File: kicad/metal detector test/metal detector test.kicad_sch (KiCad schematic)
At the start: 109 parts, among them J1 3.5mm audio jack TRS, Q1 PNP, Q2 NPN, SW1 SW_SPST, SW10 SW_SPST, SW2 SW_SPST, SW3 SW_SPST, SW4 SW_SPST, SW5 SW_SPST, SW6 SW_SPST, SW7 SW_SPST, SW8 SW_SPST, SW9 SW_SPST, U1 op amp (higher voltage), U10 3.3v lin reg, U11 lp filter, U12 op amp (lower voltage), U2 nucleo-32 uC module, U3 9v lin reg, U4 5v lin reg, U5 3.3v lin reg, U6 audio amp, U7 lp filter, U8 switch debounce, U9 5v lin reg

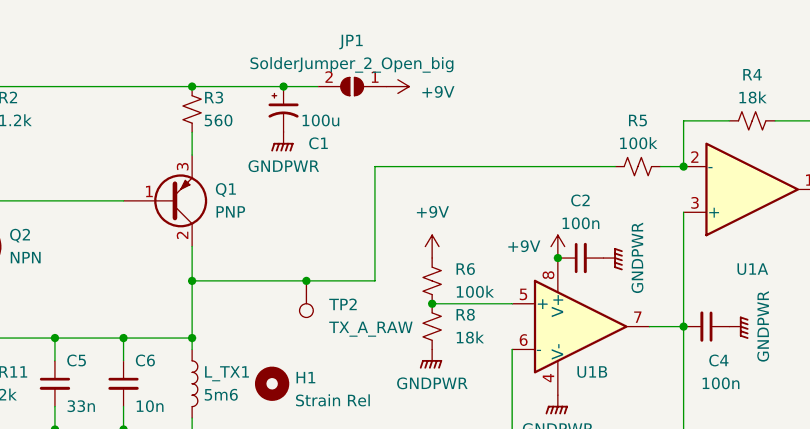
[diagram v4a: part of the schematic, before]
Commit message: Mostly positioned the parts
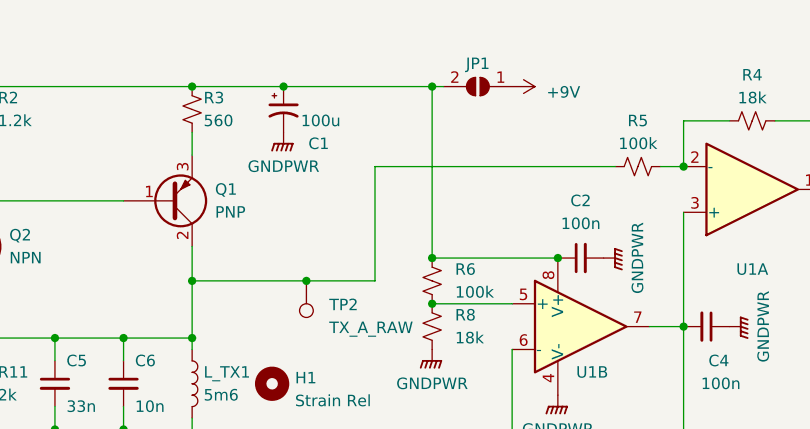
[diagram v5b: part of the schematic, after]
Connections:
- net +9V: no longer C2.1, R6.1, U1.8 (V+)
- net at C1.1, JP1.2 (B), R1.1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: now also C2.1, R6.1, U1.8 (V+)
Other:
- moved on the sheet: JP1
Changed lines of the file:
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@@
     (comment 1 "Allen Jordan, allen.jordan@gmail.com")
   )
+  (junction (at 72.39 20.32) (diameter 0) (color 0 0 0 0)
+  )
   (junction (at 45.72 48.26) (diameter 0) (color 0 0 0 0)
   )
@@
   (junction (at 22.86 20.32) (diameter 0) (color 0 0 0 0)
   )
-  (junction (at 86.36 39.37) (diameter 0) (color 0 0 0 0)
-  )
   (junction (at 109.22 100.33) (diameter 0) (color 0 0 0 0)
   )
@@
   (junction (at 40.64 90.17) (diameter 0) (color 0 0 0 0)
   )
+  (junction (at 86.36 39.37) (diameter 0) (color 0 0 0 0)
+  )
   (junction (at 247.65 110.49) (diameter 0) (color 0 0 0 0)
   )
@@
   (junction (at 240.03 48.26) (diameter 0) (color 0 0 0 0)
   )
+  (junction (at 72.39 39.37) (diameter 0) (color 0 0 0 0)
+  )
   (junction (at 38.1 58.42) (diameter 0) (color 0 0 0 0)
   )
@@
     (stroke (width 0) (type default))
   )
+  (wire (pts (xy 72.39 20.32) (xy 72.39 39.37))
+    (stroke (width 0) (type default))
+  )
   (wire (pts (xy 232.41 148.59) (xy 234.95 148.59))
     (stroke (width 0) (type default))
@@
     (stroke (width 0) (type default))
   )
-  (wire (pts (xy 59.69 20.32) (xy 55.88 20.32))
+  (wire (pts (xy 73.66 20.32) (xy 72.39 20.32))
     (stroke (width 0) (type default))
   )
@@
     (stroke (width 0) (type default))
   )
+  (wire (pts (xy 72.39 20.32) (xy 55.88 20.32))
+    (stroke (width 0) (type default))
+  )
   (wire (pts (xy 143.51 107.95) (xy 160.02 107.95))
     (stroke (width 0) (type default))
@@
     (stroke (width 0) (type default))
   )
+  (wire (pts (xy 72.39 39.37) (xy 86.36 39.37))
+    (stroke (width 0) (type default))
+  )
   (wire (pts (xy 123.19 107.95) (xy 109.22 107.95))
     (stroke (width 0) (type default))
@@
     )
   )
-  (symbol (lib_id "power:+9V") (at 67.31 20.32 270) (unit 1)
+  (symbol (lib_id "power:+9V") (at 81.28 20.32 270) (unit 1)
     (in_bom yes) (on_board yes) (dnp no) (fields_autoplaced)
-    (property "Reference" "#PWR01" (at 63.5 20.32 0)
+    (property "Reference" "#PWR01" (at 77.47 20.32 0)
       (effects (font (size 1.27 1.27)) hide)
     )
-    (property "Value" "+9V" (at 71.12 20.955 90)
+    (property "Value" "+9V" (at 85.09 20.955 90)
       (effects (font (size 1.27 1.27)) (justify left))
     )
-    (property "Footprint" "" (at 67.31 20.32 0)
+    (property "Footprint" "" (at 81.28 20.32 0)
       (effects (font (size 1.27 1.27)) hide)
     )
-    (property "Datasheet" "" (at 67.31 20.32 0)
+    (property "Datasheet" "" (at 81.28 20.32 0)
       (effects (font (size 1.27 1.27)) hide)
     )
@@
     )
   )
-  (symbol (lib_id "power:+9V") (at 86.36 39.37 0) (unit 1)
-    (in_bom yes) (on_board yes) (dnp no)
-    (property "Reference" "#PWR08" (at 86.36 43.18 0)
-      (effects (font (size 1.27 1.27)) hide)
-    )
-    (property "Value" "+9V" (at 82.55 38.1 0)
-      (effects (font (size 1.27 1.27)))
-    )
-    (property "Footprint" "" (at 86.36 39.37 0)
-      (effects (font (size 1.27 1.27)) hide)
-    )
-    (property "Datasheet" "" (at 86.36 39.37 0)
-      (effects (font (size 1.27 1.27)) hide)
-    )
-    (pin "1")
-    (instances
-      (project "metal detector test"
-        (path "/aac94249-970f-41d5-8c24-6bade512464d"
-          (reference "#PWR08") (unit 1)
-        )
-      )
-    )
-  )
   (symbol (lib_id "Device:R_Small_US") (at 17.78 48.26 270) (unit 1)
     (in_bom yes) (on_board yes) (dnp no)
@@
     )
   )
-  (symbol (lib_id "Jumper:SolderJumper_2_Open") (at 63.5 20.32 180) (unit 1)
-    (in_bom yes) (on_board yes) (dnp no) (fields_autoplaced)
-    (property "Reference" "JP1" (at 63.5 15.24 0)
+  (symbol (lib_id "Jumper:SolderJumper_2_Open") (at 77.47 20.32 180) (unit 1)
+    (in_bom yes) (on_board yes) (dnp no)
+    (property "Reference" "JP1" (at 77.47 17.78 0)
       (effects (font (size 1.27 1.27)))
     )
-    (property "Value" "SolderJumper_2_Open_big" (at 63.5 17.78 0)
-      (effects (font (size 1.27 1.27)))
+    (property "Value" "SolderJumper_2_Open_big" (at 77.47 17.78 0)
+      (effects (font (size 1.27 1.27)) hide)
     )
-    (property "Footprint" "allen footprints:SolderJumper-2_Open_big_allen" (at 63.5 20.32 0)
+    (property "Footprint" "allen footprints:SolderJumper-2_Open_big_allen" (at 77.47 20.32 0)
       (effects (font (size 1.27 1.27)) hide)
     )
-    (property "Datasheet" "~" (at 63.5 20.32 0)
+    (property "Datasheet" "~" (at 77.47 20.32 0)
       (effects (font (size 1.27 1.27)) hide)
     )
-    (property "MPN" "" (at 63.5 20.32 0)
+    (property "MPN" "" (at 77.47 20.32 0)
       (effects (font (size 1.27 1.27)) hide)
     )
@@
         )
       )
-    )
-  )
-  (symbol (lib_id "power:+9V") (at 72.39 39.37 0) (unit 1)
-    (in_bom yes) (on_board yes) (dnp no) (fields_autoplaced)
-    (property "Reference" "#PWR07" (at 72.39 43.18 0)
-      (effects (font (size 1.27 1.27)) hide)
-    )
-    (property "Value" "+9V" (at 72.39 34.29 0)
-      (effects (font (size 1.27 1.27)))
-    )
-    (property "Footprint" "" (at 72.39 39.37 0)
-      (effects (font (size 1.27 1.27)) hide)
-    )
-    (property "Datasheet" "" (at 72.39 39.37 0)
-      (effects (font (size 1.27 1.27)) hide)
-    )
-    (pin "1")
-    (instances
-      (project "metal detector test"
-        (path "/aac94249-970f-41d5-8c24-6bade512464d"
-          (reference "#PWR07") (unit 1)
-        )
-      )

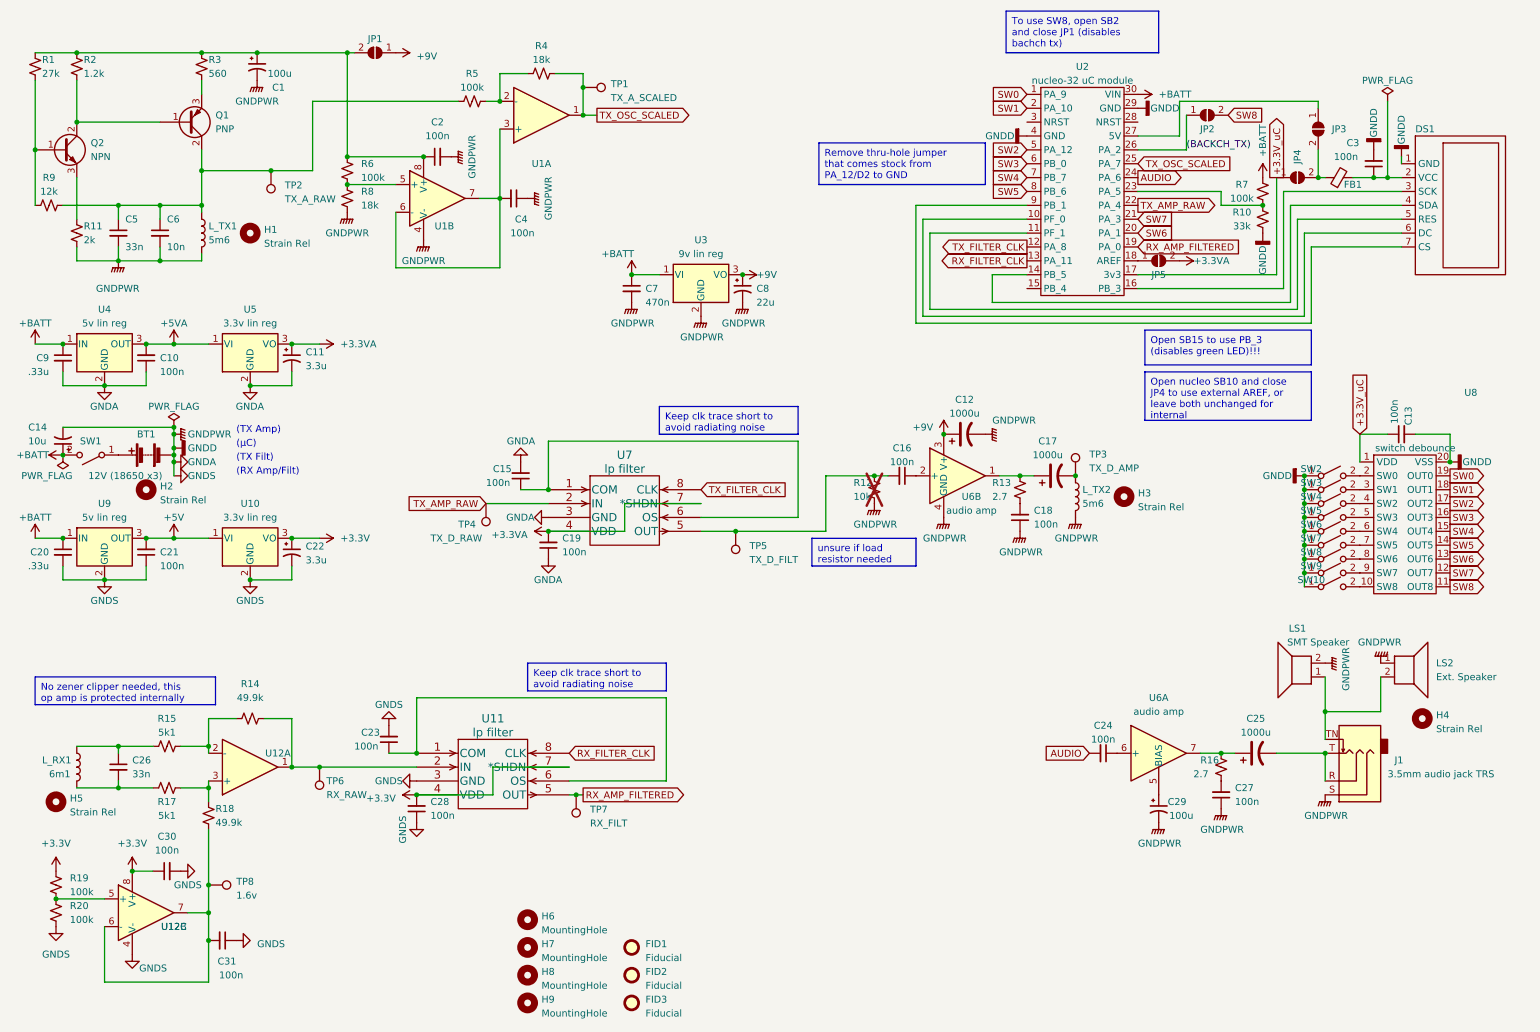
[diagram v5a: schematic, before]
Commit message: Figuring out oled and battery holder placement
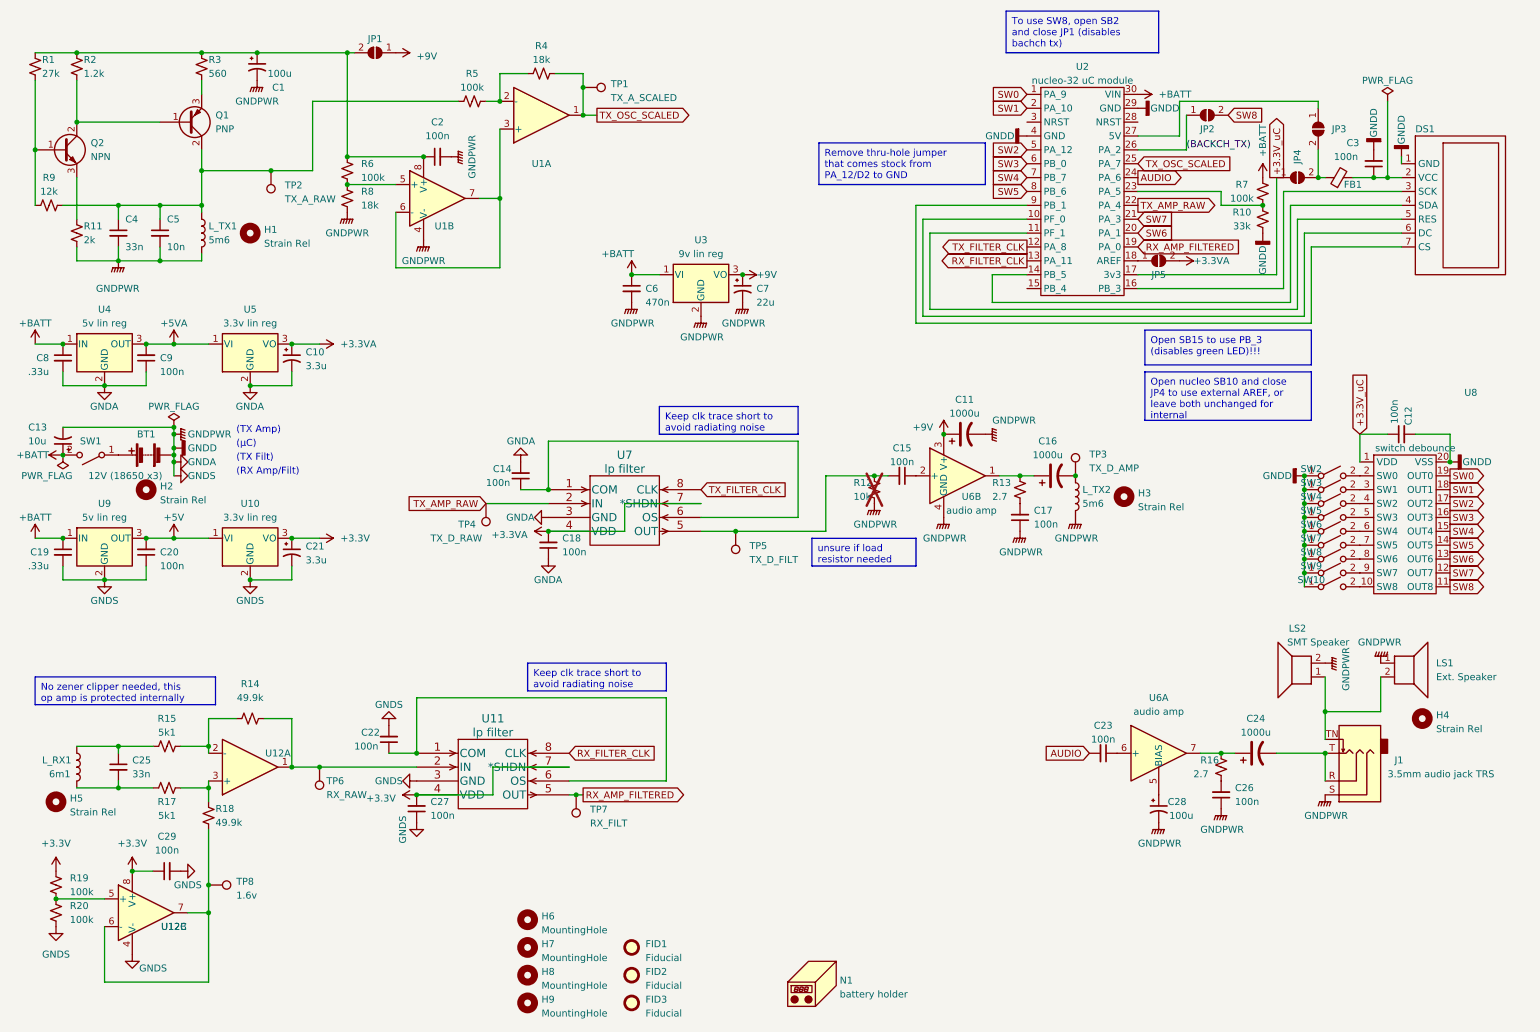
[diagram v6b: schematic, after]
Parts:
- removed C31, C4: 100n, Capacitor_SMD:C_0805_2012Metric_Pad1.18x1.45mm_HandSolder, symbol Device:C_Small
- added N1: battery holder, allen footprints:106990288_18650_x3_battery_holder, symbol Mechanical:Housing
- renumbered C11 to C10, C12 to C11, C13 to C12, C14 to C13, C15 to C14, C16 to C15, C17 to C16, C18 to C17, C19 to C18, C20 to C19, C21 to C20, C22 to C21, C23 to C22, C24 to C23, C25 to C24, C26 to C25, C27 to C26, C28 to C27, C29 to C28, C30 to C29, C5 to C4, C6 to C5, C7 to C6, C8 to C7, C9 to C8, C10 to C9, LS2 to LS1, LS1 to LS2

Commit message: working on part positions still
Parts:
- renumbered SW2 to SW0, SW3 to SW1, SW1 to SW10, SW4 to SW2, SW5 to SW3, SW6 to SW4, SW7 to SW5, SW8 to SW6, SW9 to SW7, SW10 to SW8
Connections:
- net SW0: now also U2.8 (PB_6); no longer U2.1 (PA_9)
- net SW1: now also U2.7 (PB_7); no longer U2.2 (PA_10)
- net SW2: now also U2.6 (PB_0); no longer U2.5 (PA_12)
- net SW3: now also U2.5 (PA_12); no longer U2.6 (PB_0)
- net SW4: now also U2.2 (PA_10); no longer U2.7 (PB_7)
- net SW5: now also U2.1 (PA_9); no longer U2.8 (PB_6)
- net SW6: now also JP2.2 (B); no longer U2.20 (PA_1)
- net SW8: now also U2.20 (PA_1); no longer JP2.2 (B)
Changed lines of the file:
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@@
     (effects (font (size 1.27 1.27)) (justify left top))
   )
-  (text_box "To use SW8, open SB2 and close JP1 (disables bachch tx)"
+  (text_box "To use SW6, open SB2 and close JP1 (disables bachch tx)"
     (at 193.04 12.7 0) (size 27.94 7.62)
     (stroke (width 0) (type default))
@@
     )
   )
-  (global_label "SW3" (shape input) (at 196.85 40.64 180) (fields_autoplaced)
+  (global_label "SW3" (shape input) (at 196.85 38.1 180) (fields_autoplaced)
     (effects (font (size 1.27 1.27)) (justify right))
-    (property "Intersheetrefs" "${INTERSHEET_REFS}" (at 190.0738 40.64 0)
+    (property "Intersheetrefs" "${INTERSHEET_REFS}" (at 190.0738 38.1 0)
       (effects (font (size 1.27 1.27)) (justify right) hide)
     )
@@
     )
   )
-  (global_label "SW1" (shape input) (at 196.85 30.48 180) (fields_autoplaced)
+  (global_label "SW1" (shape input) (at 196.85 43.18 180) (fields_autoplaced)
     (effects (font (size 1.27 1.27)) (justify right))
-    (property "Intersheetrefs" "${INTERSHEET_REFS}" (at 190.0738 30.48 0)
+    (property "Intersheetrefs" "${INTERSHEET_REFS}" (at 190.0738 43.18 0)
       (effects (font (size 1.27 1.27)) (justify right) hide)
     )
@@
     )
   )
-  (global_label "SW6" (shape input) (at 217.17 53.34 0) (fields_autoplaced)
+  (global_label "SW6" (shape input) (at 233.68 31.75 0) (fields_autoplaced)
     (effects (font (size 1.27 1.27)) (justify left))
-    (property "Intersheetrefs" "${INTERSHEET_REFS}" (at 223.9462 53.34 0)
+    (property "Intersheetrefs" "${INTERSHEET_REFS}" (at 240.4562 31.75 0)
       (effects (font (size 1.27 1.27)) (justify left) hide)
     )
   )
-  (global_label "SW4" (shape input) (at 196.85 43.18 180) (fields_autoplaced)
+  (global_label "SW4" (shape input) (at 196.85 30.48 180) (fields_autoplaced)
     (effects (font (size 1.27 1.27)) (justify right))
-    (property "Intersheetrefs" "${INTERSHEET_REFS}" (at 190.0738 43.18 0)
+    (property "Intersheetrefs" "${INTERSHEET_REFS}" (at 190.0738 30.48 0)
       (effects (font (size 1.27 1.27)) (justify right) hide)
     )
@@
     )
   )
-  (global_label "SW5" (shape input) (at 196.85 45.72 180) (fields_autoplaced)
+  (global_label "SW5" (shape input) (at 196.85 27.94 180) (fields_autoplaced)
     (effects (font (size 1.27 1.27)) (justify right))
-    (property "Intersheetrefs" "${INTERSHEET_REFS}" (at 190.0738 45.72 0)
+    (property "Intersheetrefs" "${INTERSHEET_REFS}" (at 190.0738 27.94 0)
       (effects (font (size 1.27 1.27)) (justify right) hide)
     )
@@
     )
   )
-  (global_label "SW8" (shape input) (at 233.68 31.75 0) (fields_autoplaced)
+  (global_label "SW8" (shape input) (at 217.17 53.34 0) (fields_autoplaced)
     (effects (font (size 1.27 1.27)) (justify left))
-    (property "Intersheetrefs" "${INTERSHEET_REFS}" (at 240.4562 31.75 0)
+    (property "Intersheetrefs" "${INTERSHEET_REFS}" (at 223.9462 53.34 0)
       (effects (font (size 1.27 1.27)) (justify left) hide)
     )
@@
     )
   )
-  (global_label "SW0" (shape input) (at 196.85 27.94 180) (fields_autoplaced)
+  (global_label "SW0" (shape input) (at 196.85 45.72 180) (fields_autoplaced)
     (effects (font (size 1.27 1.27)) (justify right))
-    (property "Intersheetrefs" "${INTERSHEET_REFS}" (at 190.0738 27.94 0)
+    (property "Intersheetrefs" "${INTERSHEET_REFS}" (at 190.0738 45.72 0)
       (effects (font (size 1.27 1.27)) (justify right) hide)
     )
   )
-  (global_label "SW2" (shape input) (at 196.85 38.1 180) (fields_autoplaced)
+  (global_label "SW2" (shape input) (at 196.85 40.64 180) (fields_autoplaced)
     (effects (font (size 1.27 1.27)) (justify right))
-    (property "Intersheetrefs" "${INTERSHEET_REFS}" (at 190.0738 38.1 0)
+    (property "Intersheetrefs" "${INTERSHEET_REFS}" (at 190.0738 40.64 0)
       (effects (font (size 1.27 1.27)) (justify right) hide)
     )
@@
   (symbol (lib_id "Switch:SW_SPST") (at 252.73 107.95 0) (unit 1)
     (in_bom yes) (on_board yes) (dnp no)
-    (property "Reference" "SW6" (at 248.92 106.68 0)
+    (property "Reference" "SW4" (at 248.92 106.68 0)
       (effects (font (size 1.27 1.27)))
     )
@@
       (project "metal detector test"
         (path "/aac94249-970f-41d5-8c24-6bade512464d"
-          (reference "SW6") (unit 1)
+          (reference "SW4") (unit 1)
         )
       )
@@
   (symbol (lib_id "Switch:SW_SPST") (at 25.4 93.98 180) (unit 1)
     (in_bom yes) (on_board yes) (dnp no)
-    (property "Reference" "SW1" (at 25.4 91.44 0)
+    (property "Reference" "SW10" (at 25.4 91.44 0)
       (effects (font (size 1.27 1.27)))
     )
@@
       (project "metal detector test"
         (path "/aac94249-970f-41d5-8c24-6bade512464d"
-          (reference "SW1") (unit 1)
+          (reference "SW10") (unit 1)
         )
       )
@@
   (symbol (lib_id "Switch:SW_SPST") (at 252.73 97.79 0) (unit 1)
     (in_bom yes) (on_board yes) (dnp no)
-    (property "Reference" "SW2" (at 248.92 96.52 0)
+    (property "Reference" "SW0" (at 248.92 96.52 0)
       (effects (font (size 1.27 1.27)))
     )
@@
       (project "metal detector test"
         (path "/aac94249-970f-41d5-8c24-6bade512464d"
-          (reference "SW2") (unit 1)
+          (reference "SW0") (unit 1)
         )
       )
@@
   (symbol (lib_id "Switch:SW_SPST") (at 252.73 118.11 0) (unit 1)
     (in_bom yes) (on_board yes) (dnp no)
-    (property "Reference" "SW10" (at 248.92 116.84 0)
+    (property "Reference" "SW8" (at 248.92 116.84 0)
       (effects (font (size 1.27 1.27)))
     )
@@
       (project "metal detector test"
         (path "/aac94249-970f-41d5-8c24-6bade512464d"
-          (reference "SW10") (unit 1)
+          (reference "SW8") (unit 1)
         )
       )
@@
   (symbol (lib_id "Switch:SW_SPST") (at 252.73 115.57 0) (unit 1)
     (in_bom yes) (on_board yes) (dnp no)
-    (property "Reference" "SW9" (at 248.92 114.3 0)
+    (property "Reference" "SW7" (at 248.92 114.3 0)
       (effects (font (size 1.27 1.27)))
     )
@@
       (project "metal detector test"
         (path "/aac94249-970f-41d5-8c24-6bade512464d"
-          (reference "SW9") (unit 1)
+          (reference "SW7") (unit 1)
         )
       )
@@
   (symbol (lib_id "Switch:SW_SPST") (at 252.73 102.87 0) (unit 1)
     (in_bom yes) (on_board yes) (dnp no)
-    (property "Reference" "SW4" (at 248.92 101.6 0)
+    (property "Reference" "SW2" (at 248.92 101.6 0)
       (effects (font (size 1.27 1.27)))
     )
@@
       (project "metal detector test"
         (path "/aac94249-970f-41d5-8c24-6bade512464d"
-          (reference "SW4") (unit 1)
+          (reference "SW2") (unit 1)
         )
       )
@@
   (symbol (lib_id "Switch:SW_SPST") (at 252.73 110.49 0) (unit 1)
     (in_bom yes) (on_board yes) (dnp no)
-    (property "Reference" "SW7" (at 248.92 109.22 0)
+    (property "Reference" "SW5" (at 248.92 109.22 0)
       (effects (font (size 1.27 1.27)))
     )
@@
       (project "metal detector test"
         (path "/aac94249-970f-41d5-8c24-6bade512464d"
-          (reference "SW7") (unit 1)
+          (reference "SW5") (unit 1)
         )
       )
@@
   (symbol (lib_id "Switch:SW_SPST") (at 252.73 113.03 0) (unit 1)
     (in_bom yes) (on_board yes) (dnp no)
-    (property "Reference" "SW8" (at 248.92 111.76 0)
+    (property "Reference" "SW6" (at 248.92 111.76 0)
       (effects (font (size 1.27 1.27)))
     )
@@
       (project "metal detector test"
         (path "/aac94249-970f-41d5-8c24-6bade512464d"
-          (reference "SW8") (unit 1)
+          (reference "SW6") (unit 1)
         )
       )
@@
   (symbol (lib_id "Switch:SW_SPST") (at 252.73 105.41 0) (unit 1)
     (in_bom yes) (on_board yes) (dnp no)
-    (property "Reference" "SW5" (at 248.92 104.14 0)
+    (property "Reference" "SW3" (at 248.92 104.14 0)
       (effects (font (size 1.27 1.27)))
     )
@@
       (project "metal detector test"
         (path "/aac94249-970f-41d5-8c24-6bade512464d"
-          (reference "SW5") (unit 1)
+          (reference "SW3") (unit 1)
         )
       )
@@
   (symbol (lib_id "Switch:SW_SPST") (at 252.73 100.33 0) (unit 1)
     (in_bom yes) (on_board yes) (dnp no)
-    (property "Reference" "SW3" (at 248.92 99.06 0)
+    (property "Reference" "SW1" (at 248.92 99.06 0)
       (effects (font (size 1.27 1.27)))
     )
@@
       (project "metal detector test"
         (path "/aac94249-970f-41d5-8c24-6bade512464d"
-          (reference "SW3") (unit 1)
+          (reference "SW1") (unit 1)
         )
       )
